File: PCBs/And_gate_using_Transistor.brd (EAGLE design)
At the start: 30 x 34.5 mm, 11 parts, among them T1 BC547, T2 BC547

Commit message: New Update
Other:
- board size 30 x 34.5 mm -> 29.5 x 34.5 mm
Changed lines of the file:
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@@
 <drawing>
 <settings>
-<setting alwaysvectorfont="yes"/>
+<setting alwaysvectorfont="no"/>
 <setting verticaltext="up"/>
 </settings>
@@
 <board>
 <plain>
-<wire x1="28.16231875" y1="34.5" x2="2.066921875" y2="34.5" width="0" layer="20"/>
-<wire x1="2.066921875" y1="34.5" x2="0" y2="32.433078125" width="0" layer="20" curve="90"/>
-<wire x1="0" y1="32.433078125" x2="0" y2="1.5111625" width="0" layer="20"/>
-<wire x1="0" y1="1.5111625" x2="1.5111625" y2="0" width="0" layer="20" curve="90"/>
-<wire x1="1.5111625" y1="0" x2="28.44391875" y2="0" width="0" layer="20"/>
+<wire x1="28.16231875" y1="34.5" x2="2.17199375" y2="34.5" width="0" layer="20"/>
+<wire x1="2.17199375" y1="34.5" x2="0.5" y2="32.82800625" width="0" layer="20" curve="90"/>
+<wire x1="0.5" y1="32.82800625" x2="0.5" y2="1.6494125" width="0" layer="20"/>
+<wire x1="0.5" y1="1.6494125" x2="2.1494125" y2="0" width="0" layer="20" curve="90"/>
+<wire x1="2.1494125" y1="0" x2="28.44391875" y2="0" width="0" layer="20"/>
 <wire x1="28.44391875" y1="0" x2="30" y2="1.55608125" width="0" layer="20" curve="90"/>
 <wire x1="30" y1="1.55608125" x2="30" y2="32.66231875" width="0" layer="20"/>
 <wire x1="30" y1="32.66231875" x2="28.16231875" y2="34.5" width="0" layer="20" curve="90"/>
-<hole x="2" y="2" drill="3"/>
-<hole x="27.984" y="2" drill="3"/>
-<hole x="28.063" y="32.365" drill="3"/>
-<hole x="2.103" y="32.492" drill="3"/>
-<text x="3" y="6" size="1.778" layer="21" rot="R90">Pinwheel Robotics </text>
+<hole x="2.5" y="2" drill="3"/>
+<hole x="28" y="2" drill="3"/>
+<hole x="28" y="32.5" drill="3"/>
+<hole x="2.5" y="32.492" drill="3"/>
+<text x="3.508" y="7.143" size="1.778" layer="21" rot="R90">Pinwheel Robotics </text>
 <text x="29.5" y="25" size="1.778" layer="22" rot="MR270">care@pinwheel</text>
 </plain>

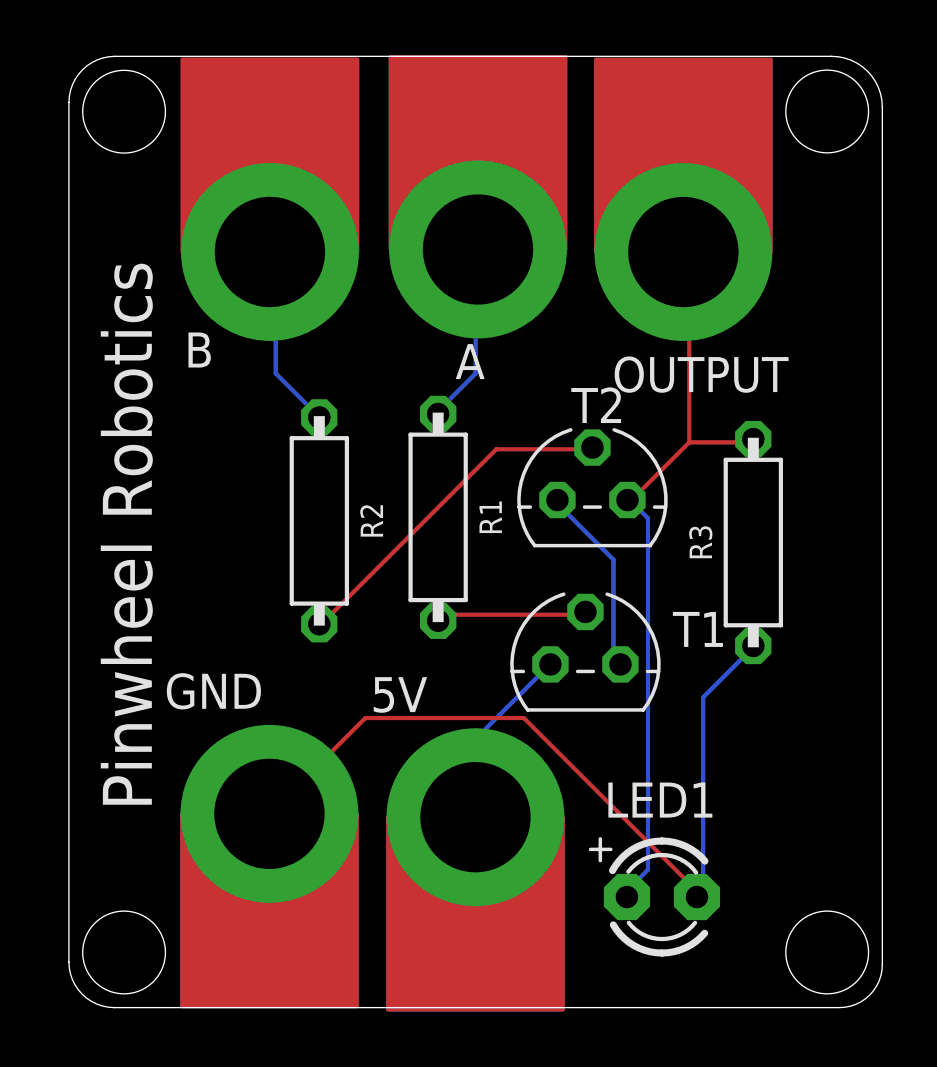
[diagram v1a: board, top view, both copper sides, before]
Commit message: New Update for board curv
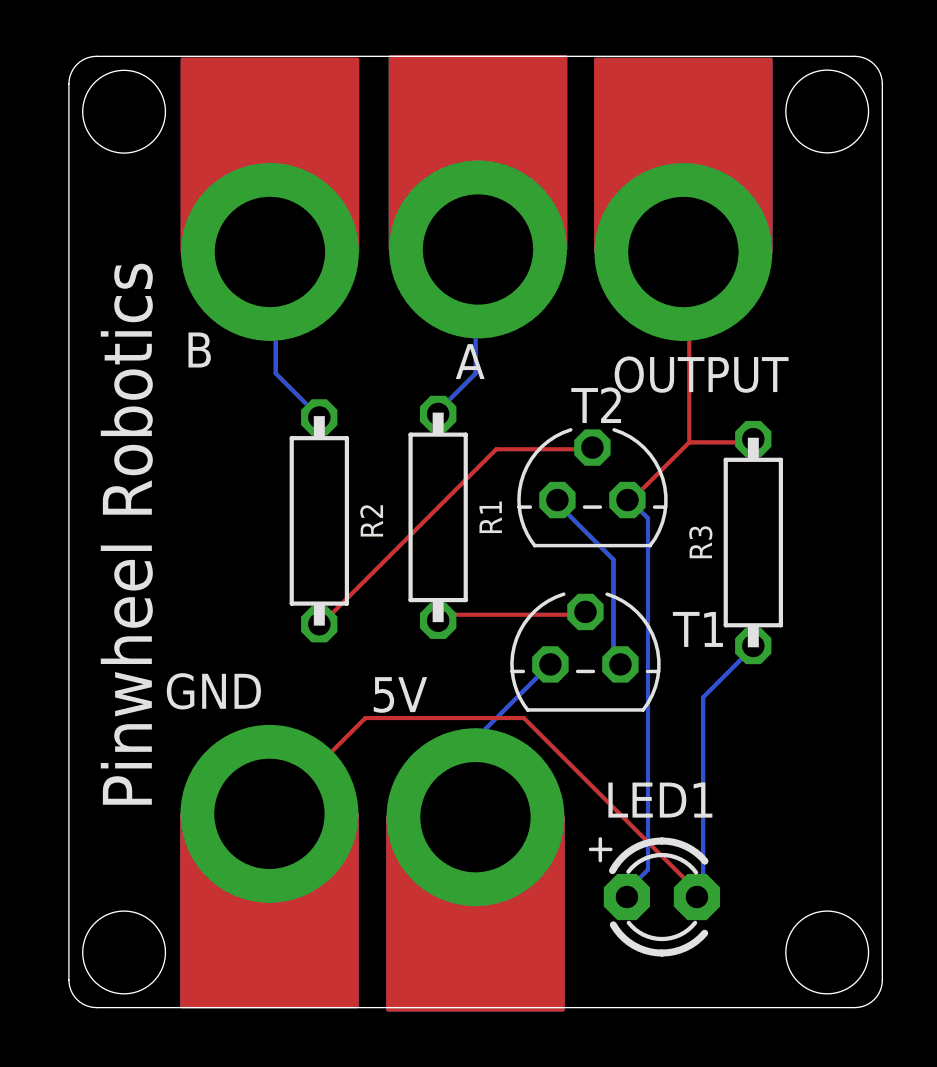
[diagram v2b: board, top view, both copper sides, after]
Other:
- outline, holes or cut-outs redrawn
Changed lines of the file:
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@@
 <drawing>
 <settings>
-<setting alwaysvectorfont="no"/>
+<setting alwaysvectorfont="yes"/>
 <setting verticaltext="up"/>
 </settings>
@@
 <board>
 <plain>
-<wire x1="28.16231875" y1="34.5" x2="2.17199375" y2="34.5" width="0" layer="20"/>
-<wire x1="2.17199375" y1="34.5" x2="0.5" y2="32.82800625" width="0" layer="20" curve="90"/>
-<wire x1="0.5" y1="32.82800625" x2="0.5" y2="1.6494125" width="0" layer="20"/>
-<wire x1="0.5" y1="1.6494125" x2="2.1494125" y2="0" width="0" layer="20" curve="90"/>
-<wire x1="2.1494125" y1="0" x2="28.44391875" y2="0" width="0" layer="20"/>
-<wire x1="28.44391875" y1="0" x2="30" y2="1.55608125" width="0" layer="20" curve="90"/>
-<wire x1="30" y1="1.55608125" x2="30" y2="32.66231875" width="0" layer="20"/>
-<wire x1="30" y1="32.66231875" x2="28.16231875" y2="34.5" width="0" layer="20" curve="90"/>
+<wire x1="0.5" y1="33.5" x2="0.5" y2="1" width="0" layer="20"/>
+<wire x1="0.5" y1="1" x2="1.5" y2="0" width="0" layer="20" curve="90"/>
+<wire x1="1.5" y1="0" x2="29" y2="0" width="0" layer="20"/>
+<wire x1="29" y1="0" x2="30" y2="1" width="0" layer="20" curve="90"/>
+<wire x1="30" y1="1" x2="30" y2="33.5" width="0" layer="20"/>
+<wire x1="30" y1="33.5" x2="29" y2="34.5" width="0" layer="20" curve="90"/>
+<wire x1="29" y1="34.5" x2="1.5" y2="34.5" width="0" layer="20"/>
+<wire x1="1.5" y1="34.5" x2="0.5" y2="33.5" width="0" layer="20" curve="90"/>
 <hole x="2.5" y="2" drill="3"/>
 <hole x="28" y="2" drill="3"/>

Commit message: Dimension added
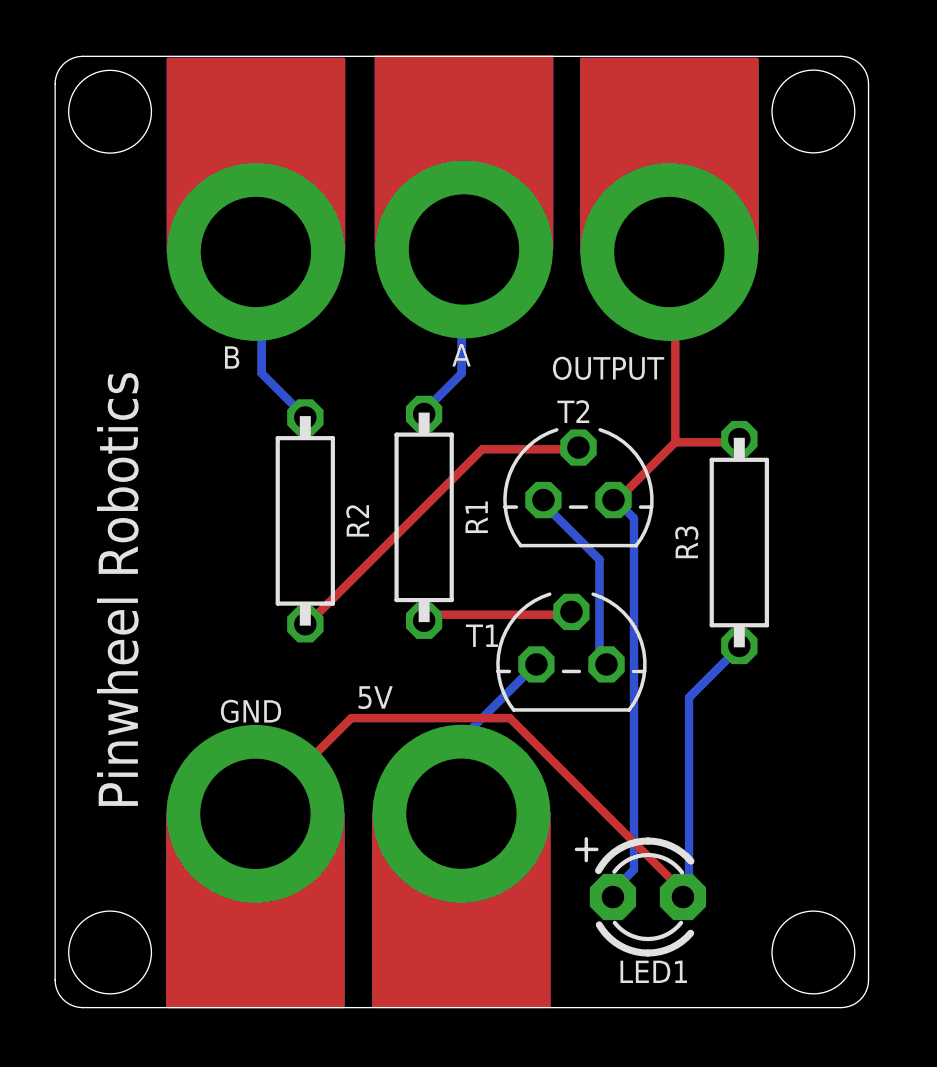
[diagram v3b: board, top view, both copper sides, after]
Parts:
- moved 5V 0.52 mm to (14.7, 7.03)
- moved LED1 0.51 mm to (21.5, 4.01)
- moved R3 0.51 mm to (24.8, 16.9)
- moved A 0.51 mm to (14.8, 27.5)
- moved R1 0.51 mm to (13.4, 17.8)
- moved B 0.51 mm to (7.28, 27.4)
- moved GND 0.51 mm to (7.26, 7.03)
- moved OUTPUT 0.51 mm to (22.3, 27.4)
- moved R2 0.51 mm to (9.07, 17.7)
- moved T1 0.51 mm to (18.7, 12.4)
- moved T2 0.51 mm to (19.0, 18.4)
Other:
- board text added: "care@pinwheel.in"
- board text removed: "care@pinwheel"
